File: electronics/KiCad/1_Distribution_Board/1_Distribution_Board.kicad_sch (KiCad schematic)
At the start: 10 parts, among them J19 Conn_01x06, J6 Conn_01x10, Q5 DMG2305UX, SW1 SW_Push

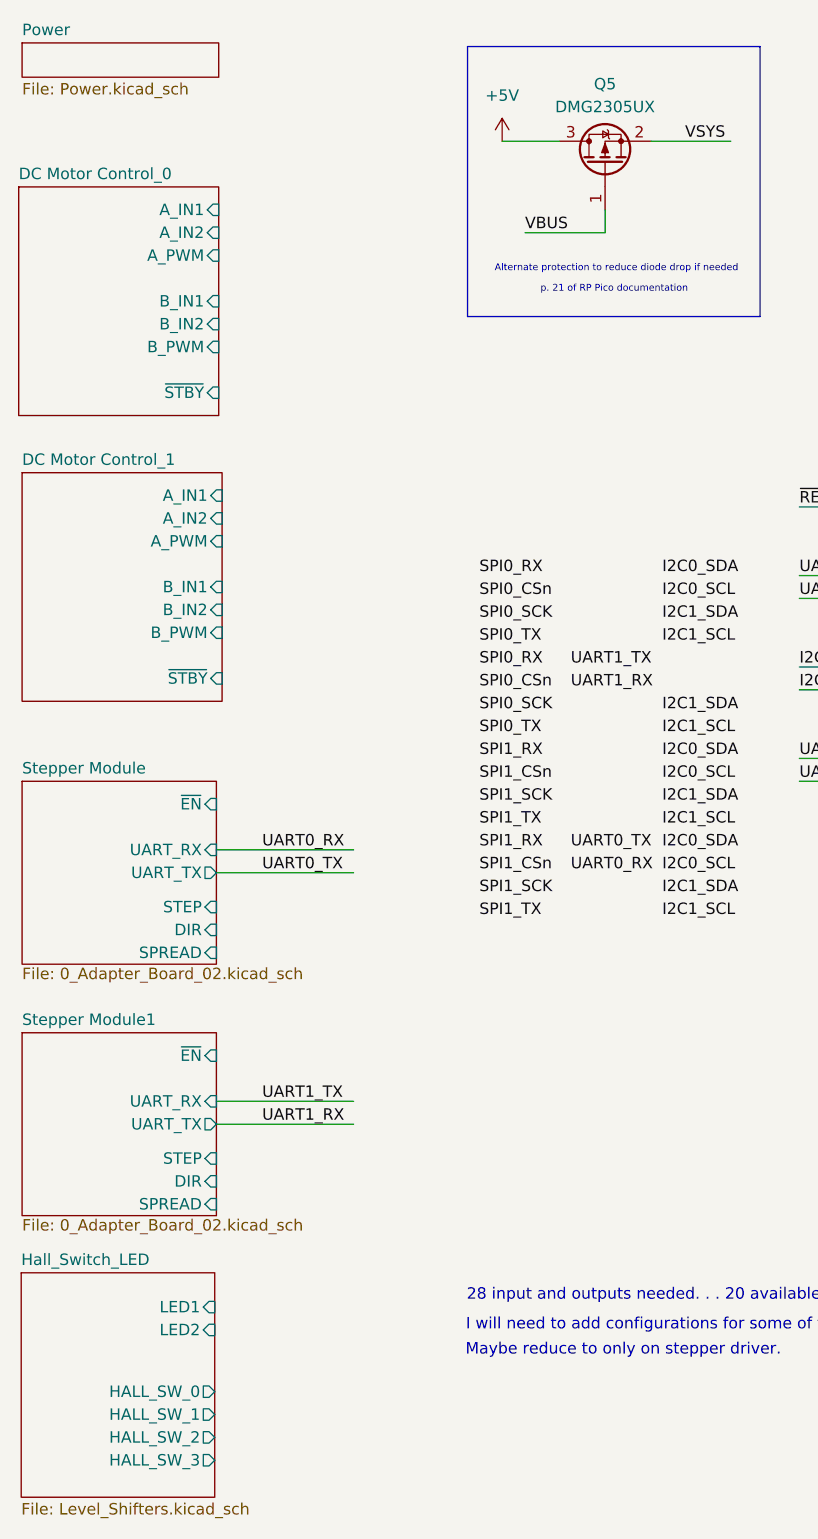
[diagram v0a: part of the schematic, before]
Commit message: Updated schematics
Updated to remove additional stepper drive, corrected short on hall circuit. Removed level shifters for PWM signals.
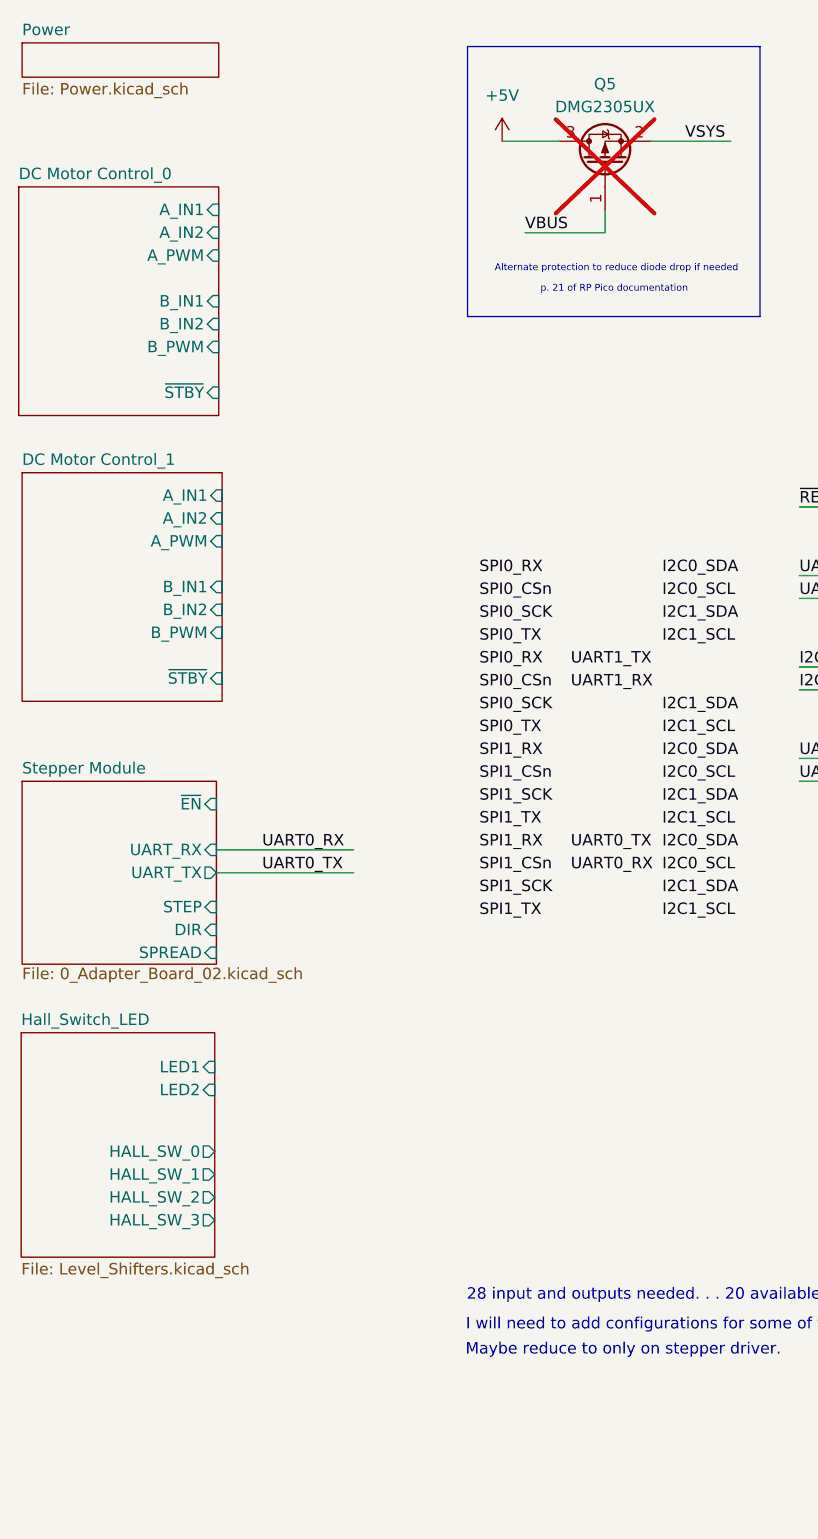
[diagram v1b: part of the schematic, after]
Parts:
- Q5: now not fitted
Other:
- removed sheet Stepper Module1
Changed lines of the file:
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@@
 	(wire
 		(pts
-			(xy 41.91 135.89) (xy 57.15 135.89)
-		)
-		(stroke
-			(width 0)
-			(type default)
-		)
-	)
-	(wire
-		(pts
-			(xy 41.91 133.35) (xy 57.15 133.35)
-		)
-		(stroke
-			(width 0)
-			(type default)
-		)
-	)
-	(wire
-		(pts
 			(xy 260.35 121.92) (xy 250.19 121.92)
 		)
@@
 		)
 	)
-	(label "UART1_RX"
-		(at 46.99 135.89 0)
-		(effects
-			(font
-				(size 1.27 1.27)
-			)
-			(justify left bottom)
-		)
-	)
 	(label "SPI1_TX"
 		(at 71.12 113.03 0)
@@
 		)
 	)
-	(label "UART1_TX"
-		(at 46.99 133.35 0)
-		(effects
-			(font
-				(size 1.27 1.27)
-			)
-			(justify left bottom)
-		)
-	)
 	(label "I2C0_SCL"
 		(at 91.44 77.47 0)
@@
 		(in_bom yes)
 		(on_board yes)
-		(dnp no)
+		(dnp yes)
 		(fields_autoplaced yes)
 		(property "Reference" "Q5"
@@
 			(project "1_Distribution_Board"
 				(path "/d53c8c01-e754-4310-8a73-7d7c95e64cd3"
-					(page "7")
+					(page "4")
 				)
 			)
@@
 			(project "1_Distribution_Board"
 				(path "/d53c8c01-e754-4310-8a73-7d7c95e64cd3"
-					(page "4")
-				)
-			)
-		)
-	)
-	(sheet
-		(at 20.32 125.73)
-		(size 21.59 20.32)
-		(exclude_from_sim no)
-		(in_bom yes)
-		(on_board yes)
-		(dnp no)
-		(fields_autoplaced yes)
-		(stroke
-			(width 0.1524)
-			(type solid)
-		)
-		(fill
-			(color 0 0 0 0.0000)
-		)
-		(property "Sheetname" "Stepper Module1"
-			(at 20.32 125.0184 0)
-			(effects
-				(font
-					(size 1.27 1.27)
-				)
-				(justify left bottom)
-			)
-		)
-		(property "Sheetfile" "0_Adapter_Board_02.kicad_sch"
-			(at 20.32 146.3796 0)
-			(effects
-				(font
-					(size 1.27 1.27)
-				)
-				(justify left top)
-			)
-		)
-		(pin "DIR" input
-			(at 41.91 142.24 0)
-			(effects
-				(font
-					(size 1.27 1.27)
-				)
-				(justify right)
-			)
-		)
-		(pin "SPREAD" input
-			(at 41.91 144.78 0)
-			(effects
-				(font
-					(size 1.27 1.27)
-				)
-				(justify right)
-			)
-		)
-		(pin "STEP" input
-			(at 41.91 139.7 0)
-			(effects
-				(font
-					(size 1.27 1.27)
-				)
-				(justify right)
-			)
-		)
-		(pin "UART_RX" input
-			(at 41.91 133.35 0)
-			(effects
-				(font
-					(size 1.27 1.27)
-				)
-				(justify right)
-			)
-		)
-		(pin "UART_TX" output
-			(at 41.91 135.89 0)
-			(effects
-				(font
-					(size 1.27 1.27)
-				)
-				(justify right)
-			)
-		)
-		(pin "~{EN}" input
-			(at 41.91 128.27 0)
-			(effects
-				(font
-					(size 1.27 1.27)
-				)
-				(justify right)
-			)
-		)
-		(instances
-			(project "1_Distribution_Board"
-				(path "/d53c8c01-e754-4310-8a73-7d7c95e64cd3"
 					(page "3")
 				)
@@
 	)
 	(sheet
-		(at 20.221 152.4)
+		(at 20.221 125.73)
 		(size 21.5 24.938)
 		(exclude_from_sim no)
@@
 		)
 		(property "Sheetname" "Hall_Switch_LED"
-			(at 20.221 151.6884 0)
+			(at 20.221 125.0184 0)
 			(effects
 				(font
@@
 		)
 		(property "Sheetfile" "Level_Shifters.kicad_sch"
-			(at 20.221 177.9226 0)
+			(at 20.221 151.2526 0)
 			(effects
 				(font
@@
 		)
 		(pin "HALL_SW_0" output
-			(at 41.721 165.608 0)
+			(at 41.721 138.938 0)
 			(effects
 				(font
@@
 		)
 		(pin "HALL_SW_1" output
-			(at 41.721 168.148 0)
+			(at 41.721 141.478 0)
 			(effects
 				(font
@@
 		)
 		(pin "HALL_SW_2" output
-			(at 41.721 170.688 0)
+			(at 41.721 144.018 0)
 			(effects
 				(font
@@
 		)
 		(pin "HALL_SW_3" output
-			(at 41.721 173.228 0)
+			(at 41.721 146.558 0)
 			(effects
 				(font
@@
 		)
 		(pin "LED1" input
-			(at 41.721 156.21 0)
+			(at 41.721 129.54 0)
 			(effects
 				(font
@@
 		)
 		(pin "LED2" input
-			(at 41.721 158.75 0)
+			(at 41.721 132.08 0)
 			(effects
 				(font

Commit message: footprint additions
Added Footprints to resistors and most components.
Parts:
- D4: footprint (none) -> PCM_SparkFun-Semiconductor-Standard:SOD-123
- R25, R3, R4: footprint (none) -> Resistor_SMD:R_0805_2012Metric_Pad1.20x1.40mm_HandSolder
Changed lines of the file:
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@@
 			)
 		)
-		(property "Footprint" ""
+		(property "Footprint" "Resistor_SMD:R_0805_2012Metric_Pad1.20x1.40mm_HandSolder"
 			(at 211.836 75.184 90)
 			(effects
@@
 			)
 		)
-		(property "Footprint" ""
+		(property "Footprint" "Resistor_SMD:R_0805_2012Metric_Pad1.20x1.40mm_HandSolder"
 			(at 224.536 75.184 90)
 			(effects
@@
 			)
 		)
-		(property "Footprint" ""
+		(property "Footprint" "PCM_SparkFun-Semiconductor-Standard:SOD-123"
 			(at 127 43.18 0)
 			(effects
@@
 			)
 		)
-		(property "Footprint" ""
+		(property "Footprint" "Resistor_SMD:R_0805_2012Metric_Pad1.20x1.40mm_HandSolder"
 			(at 219.456 30.734 90)
 			(effects

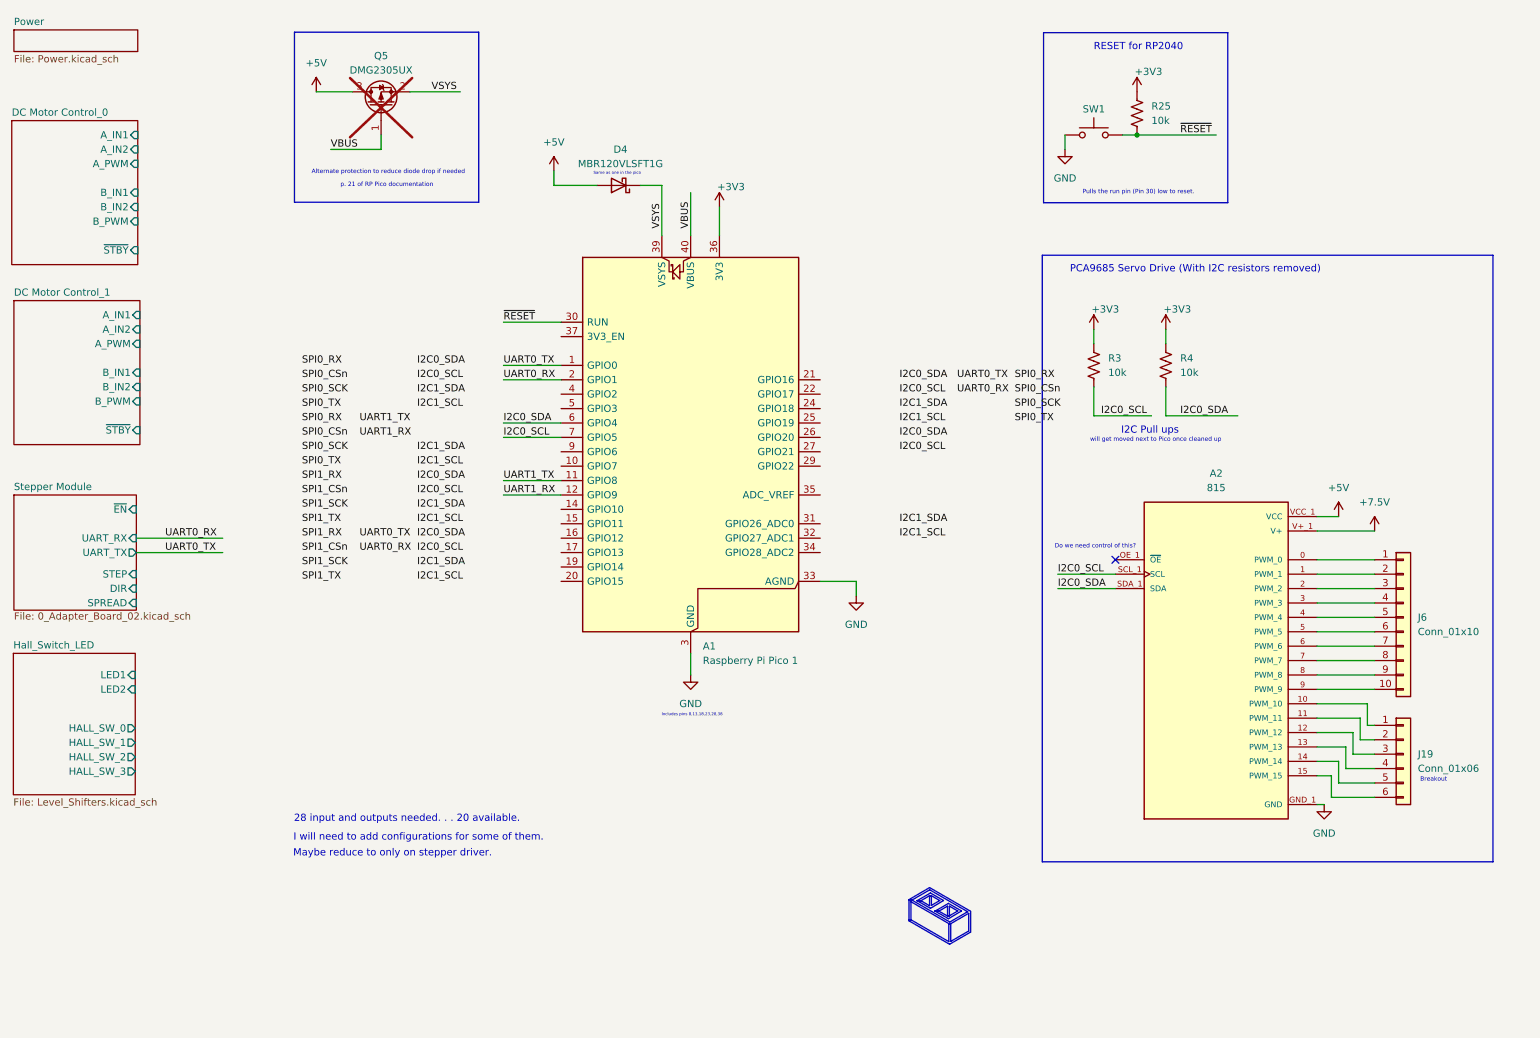
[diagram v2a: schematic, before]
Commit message: Updated to add 2 more steppers
Updated to add two more steppers, dual with the motor controllers. they will be either or. Layout hole pattern started. Still need some footprints assigned.
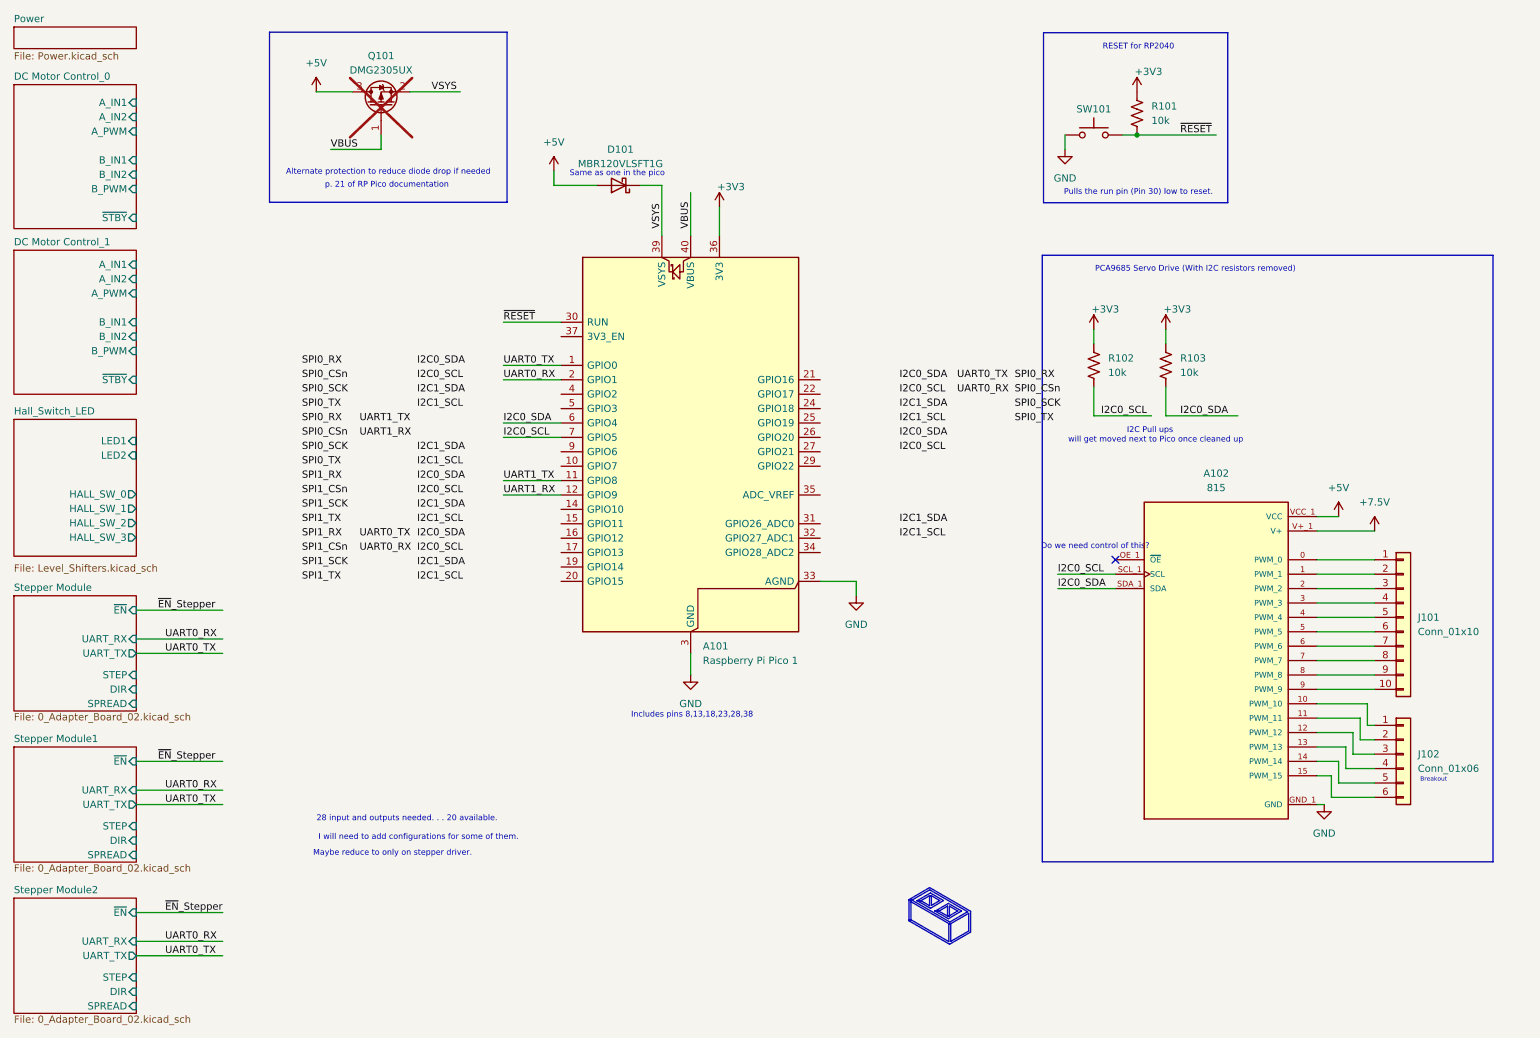
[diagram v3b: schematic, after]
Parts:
- renumbered A1 to A101, A2 to A102, D4 to D101, J6 to J101, J19 to J102, Q5 to Q101, R25 to R101, R3 to R102, R4 to R103, SW1 to SW101
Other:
- added sheet Stepper Module1 (0_Adapter_Board_02.kicad_sch)
- added sheet Stepper Module2 (0_Adapter_Board_02.kicad_sch)

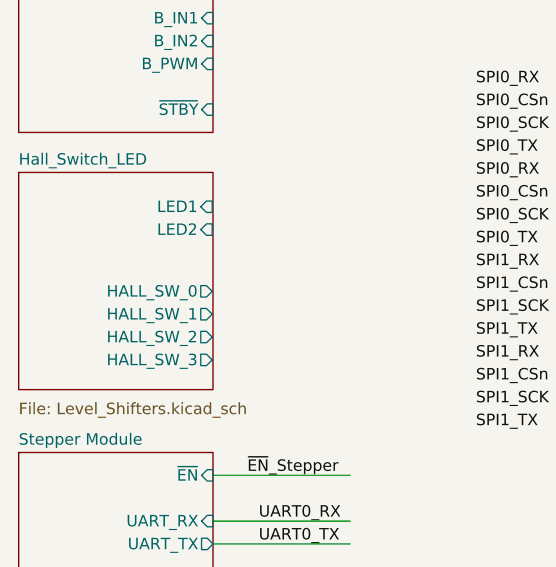
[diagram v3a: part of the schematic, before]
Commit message: Updated power page to use RECOM modules
Updated to use RECOM modules or alternated from JLPCB same footprint, gets us going. Also added conenctors.
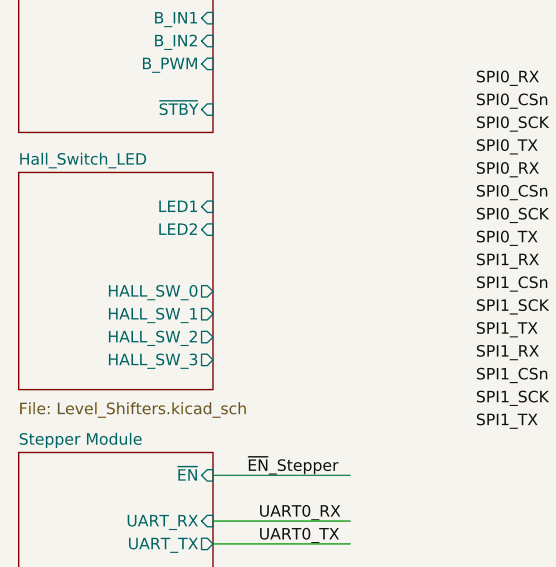
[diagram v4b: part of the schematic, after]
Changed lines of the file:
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@@
 		)
 		(pin "HALL_SW_0" output
-			(at 41.82 97.663 0)
+			(at 41.91 97.663 0)
 			(effects
 				(font
@@
 		)
 		(pin "HALL_SW_1" output
-			(at 41.82 100.203 0)
+			(at 41.91 100.203 0)
 			(effects
 				(font
@@
 		)
 		(pin "HALL_SW_2" output
-			(at 41.82 102.743 0)
+			(at 41.91 102.743 0)
 			(effects
 				(font
@@
 		)
 		(pin "HALL_SW_3" output
-			(at 41.82 105.283 0)
+			(at 41.91 105.283 0)
 			(effects
 				(font
@@
 		)
 		(pin "LED1" input
-			(at 41.82 88.265 0)
+			(at 41.91 88.265 0)
 			(effects
 				(font
@@
 		)
 		(pin "LED2" input
-			(at 41.82 90.805 0)
+			(at 41.91 90.805 0)
 			(effects
 				(font
